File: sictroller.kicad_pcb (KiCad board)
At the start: 8 copper layers, 297 parts, among them J1 CONN_01X02, J10 CONN_01X02, J11 RINGTERM, J12 RINGTERM, J13 CONN_01X01, J2 CONN_01X08, J3 CONN_02X05, J4 RINGTERM, J5 RINGTERM, J6 RINGTERM, J7 CONN_01X02, J8 RINGTERM, J9 RINGTERM, P1 CONN_01X03, Q1 CSD17483F4, Q2 CCS050M12CM2, T1 7508110151, U1 ACPL-M61L, U10 74LVC2G04, U11 TXS0108E, U12 MGJ1, U13 MGJ1, U14 2ED020I12-F2, U15 MGJ1, U16 MGJ1, U17 2ED020I12-F2, U18 MGJ1, U19 MGJ1, U2 TMS320F28069M, U20 2ED020I12-F2, U3 ADM3053, U4 TPS76201, U5 TPS76201, U6 XCL221B18, U7 VIPER26HD, U8 ADUM5241, U9 MAX6691, Y1 CSTCE20M0V13C

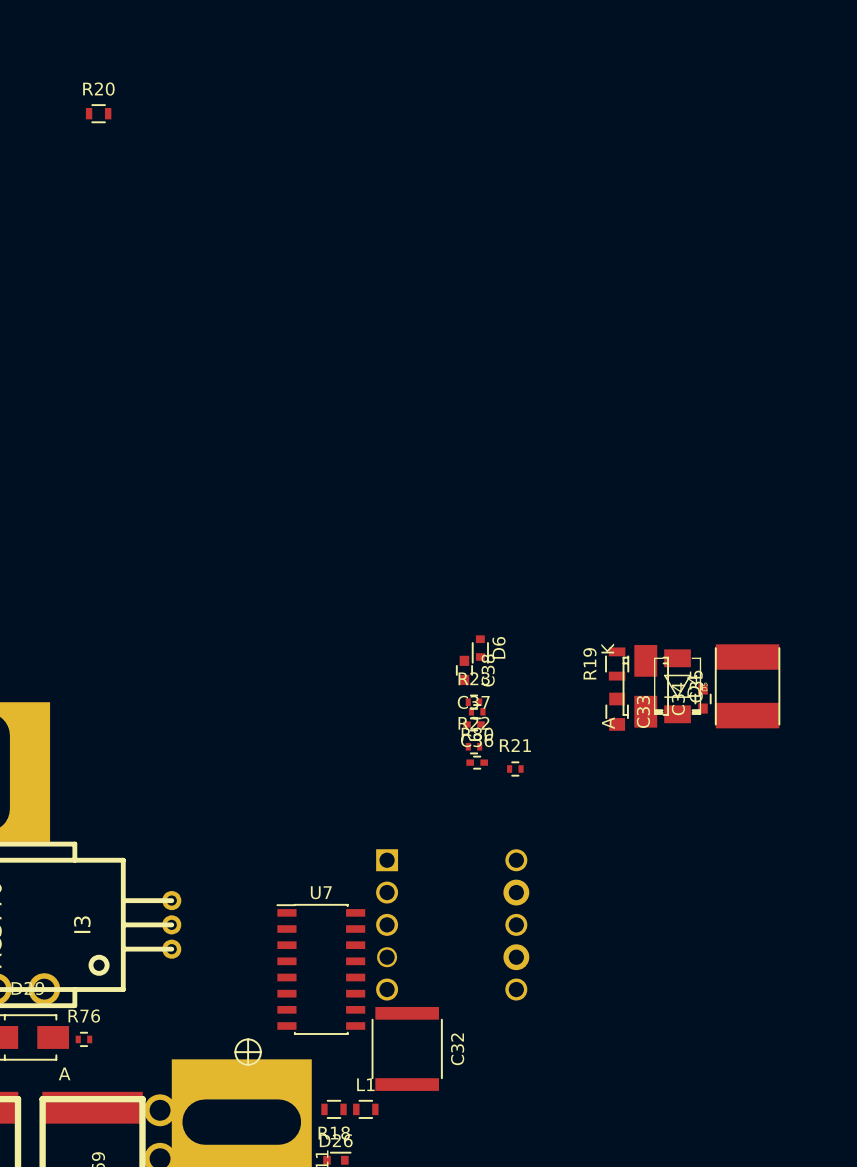
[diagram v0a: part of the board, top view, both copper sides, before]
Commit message: stepdown PSU placed
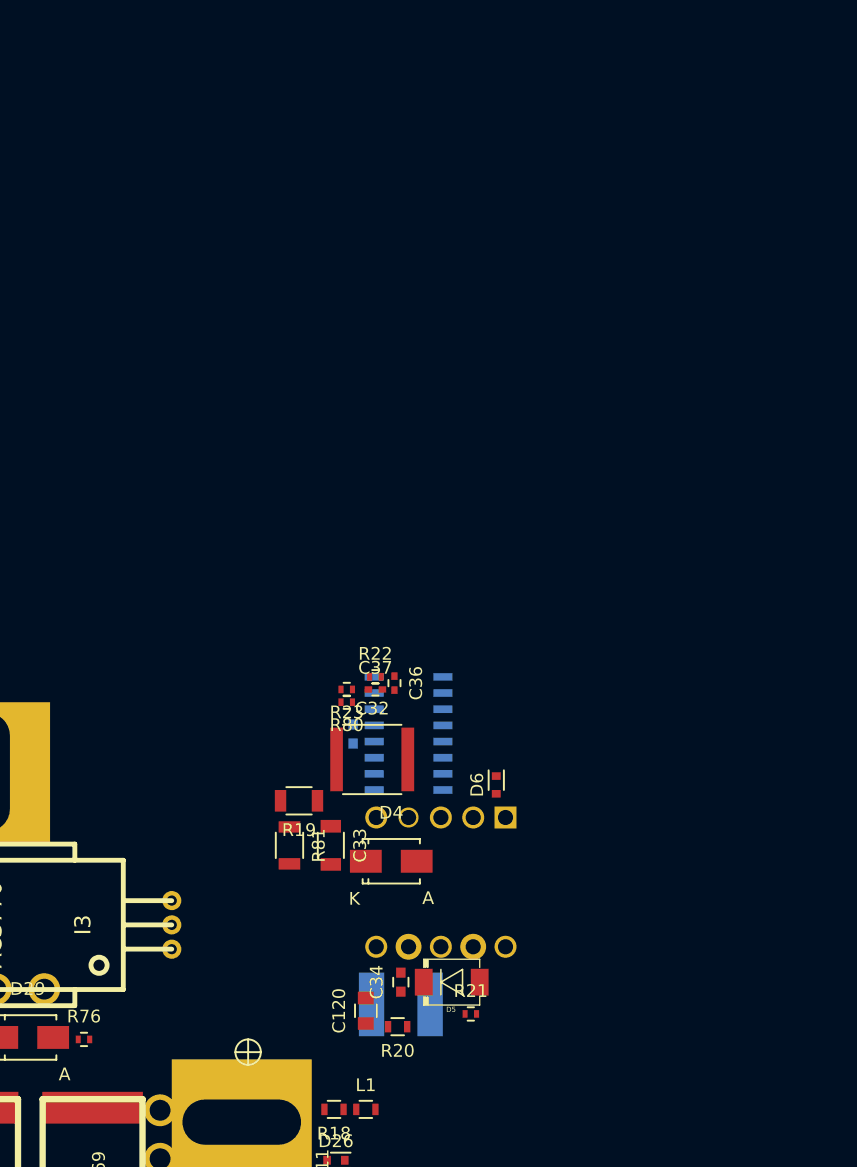
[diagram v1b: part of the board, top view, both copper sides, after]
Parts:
- added C120: 10uF 16V, Capacitors_SMD:C_0805, F.Cu at (162.2, 50.8)
- added R81: 51k, Resistors_SMD:R_1206, F.Cu at (156.2, 37.8)
- C32: value 1uF 700V -> 0.47uF 1kV
- C33: footprint Capacitors_SMD:C_0805 -> Capacitors_SMD:C_1206
- C35, C38, U7: moved to B.Cu
- R19: value 100k -> 51k; footprint Resistors_SMD:R_0805 -> Resistors_SMD:R_1206
- R20: value 0R/BEAD -> FERRITE
- moved R20 75.5 mm to (164.8, 52.0), turned to 180 degrees
- moved C35 37.0 mm to (165.0, 50.2), turned to 180 degrees
- moved C34 32.5 mm to (165.0, 48.5)
- moved D5 29.3 mm to (169.0, 48.5), turned to 0 degrees
- moved R19 27.2 mm to (157.0, 34.2), turned to 180 degrees
- moved C33 24.8 mm to (159.5, 37.8)
- moved D4 24.3 mm to (164.2, 39.0), turned to 0 degrees
- moved C32 22.9 mm to (162.8, 31.0), turned to 0 degrees
- moved U7 19.8 mm to (165.6, 29.0)
- moved R21 19.6 mm to (170.5, 51.0)
- moved D6 10.8 mm to (172.5, 33.0), turned to 90 degrees
- moved R80 10.3 mm to (160.8, 26.5)
- moved C38 10.1 mm to (161.2, 29.0)
- moved R23 10.0 mm to (160.8, 25.5), turned to 180 degrees
- moved R22 9.50 mm to (163.0, 24.5)
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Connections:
- R19 pad 2: Net-(C33-Pad2) -> Net-(R19-Pad2)
- U11 pad 9: +3V3 -> (no net)

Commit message: Add more ceralinks on rear
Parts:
- removed the R20 at (164.8, 52.0)
- added C79: 1uF, sictroller:Ceralink-L, B.Cu at (82.1, 63.1)
- added C80: 1uF, sictroller:Ceralink-L, B.Cu at (91.8, 63.1)
- added C81: 1uF, sictroller:Ceralink-L, B.Cu at (101.6, 63.1)
- added C82: 1uF, sictroller:Ceralink-L, B.Cu at (111.4, 63.1)
- added C83: 1uF, sictroller:Ceralink-L, B.Cu at (121.2, 63.1)
- added C84: 1uF, sictroller:Ceralink-L, B.Cu at (131.0, 63.1)
- added C85: 1uF, sictroller:Ceralink-L, B.Cu at (82.1, 77.0)
- added C86: 1uF, sictroller:Ceralink-L, B.Cu at (91.8, 77.0)
- added C87: 1uF, sictroller:Ceralink-L, B.Cu at (101.6, 77.0)
- added C88: 1uF, sictroller:Ceralink-L, B.Cu at (111.4, 77.0)
- added C89: 1uF, sictroller:Ceralink-L, B.Cu at (121.2, 77.0)
- added C90: 1uF, sictroller:Ceralink-L, B.Cu at (131.0, 77.0)
- added R21: FERRITE, Resistors_SMD:R_0805, F.Cu at (164.8, 52.0)
- added TH2: NCP15XW153J03RC, Resistors_SMD:R_0402, B.Cu at (106.5, 70.0)
- added W23: TEST_1P, Measurement_Points:Measurement_Point_Round-TH_Small, F.Cu at (160.8, 103.8)
- added W24: TEST_1P, Measurement_Points:Measurement_Point_Round-TH_Small, F.Cu at (170.8, 103.8)
- moved U8 165.6 mm to (163.8, 108.0)
- moved J10 160.7 mm to (164.5, 96.8)
- moved U9 158.4 mm to (164.7, 100.9)
- moved R48 151.2 mm to (164.5, 103.5)
- moved R37 30.9 mm to (62.5, -44.2)
- moved R36 28.7 mm to (58.0, -44.8)
- moved C48 18.7 mm to (59.2, -40.5)
- moved R46 10.4 mm to (89.8, -20.0)
- moved R38 8.14 mm to (91.0, -25.0)
- moved R31 6.19 mm to (87.2, -19.2)
- moved C42 4.36 mm to (62.5, -29.8)
- moved C46 3.10 mm to (62.0, -34.0)
- turned C76 to 90 degrees
- renumbered C87 to C100, C88 to C101, C89 to C102, C90 to C103, C91 to C104, C92 to C105, C93 to C106, C94 to C107, C95 to C108, C96 to C109, C97 to C110, C98 to C111, C99 to C112, C100 to C113, C101 to C114, C102 to C115, C103 to C116, C104 to C117, C105 to C118, C106 to C119, C107 to C120, C108 to C121, C109 to C122, C110 to C123, C111 to C124, C112 to C125, C113 to C126, C114 to C127, C115 to C128, C116 to C129, C117 to C130, C118 to C131, C119 to C132, C120 to C35, C35 to C36, C36 to C37, C37 to C38, C38 to C39, C39 to C40, C40 to C41, C41 to C42, C42 to C43, C43 to C44, C44 to C45, C45 to C46, C46 to C47, C47 to C48, C48 to C49, C49 to C50, C50 to C51, C51 to C52, C52 to C53, C53 to C54, C54 to C55, C55 to C56, C56 to C57, C57 to C58, C58 to C59, C59 to C60, C60 to C61, C61 to C62, C62 to C63, C63 to C64, C64 to C65, C65 to C66, C66 to C67, C67 to C68, C68 to C69, C69 to C70, C70 to C71, C71 to C72, C72 to C73, C73 to C74, C74 to C75, C75 to C76, C76 to C77, C77 to C78, C78 to C91, C79 to C92, C80 to C93, C81 to C94, C82 to C95, C83 to C96, C84 to C97, C85 to C98, C86 to C99, R81 to R20, R21 to R22, R80 to R23, R22 to R24, R23 to R25, R24 to R26, R25 to R27, R26 to R28, R27 to R29, R28 to R30, R29 to R31, R30 to R32, R31 to R33, R32 to R34, R33 to R35, R34 to R36, R35 to R37, R36 to R38, R37 to R39, R38 to R40, R39 to R41, R40 to R42, R41 to R43, R42 to R44, R43 to R45, R44 to R46, R45 to R47, R46 to R48, R47 to R49, R48 to R50, R49 to R51, R50 to R52, R51 to R53, R52 to R54, R53 to R55, R54 to R56, R55 to R57, R56 to R58, R57 to R59, R58 to R60, R59 to R61, R60 to R62, R61 to R63, R62 to R64, R63 to R65, R64 to R66, R65 to R67, R66 to R68, R67 to R69, R68 to R70, R69 to R71, R70 to R72, R71 to R73, R72 to R74, R73 to R75, R74 to R76, R75 to R77, R76 to R78, R77 to R79, R78 to R80, R79 to R81
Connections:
- TH1 pad 2: CCS_NTC_2 -> Net-(TH1-Pad2)
- U9 pad 4: Net-(TH1-Pad1) -> Net-(U9-Pad4)
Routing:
- net CCS_NTC_2: track 13.7 -> 0.00 mm
- net Net-(TH1-Pad1): track 13.7 -> 0.60 mm, vias 0 -> 1
- net Net-(TH1-Pad2): track 0.00 -> 0.60 mm, vias 0 -> 1
- added copper zone on F.Cu, net BUS+
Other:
- rule via_min_drill: 0.254 -> 0.2032
- rule via_min_size: 0.635 -> 0.381

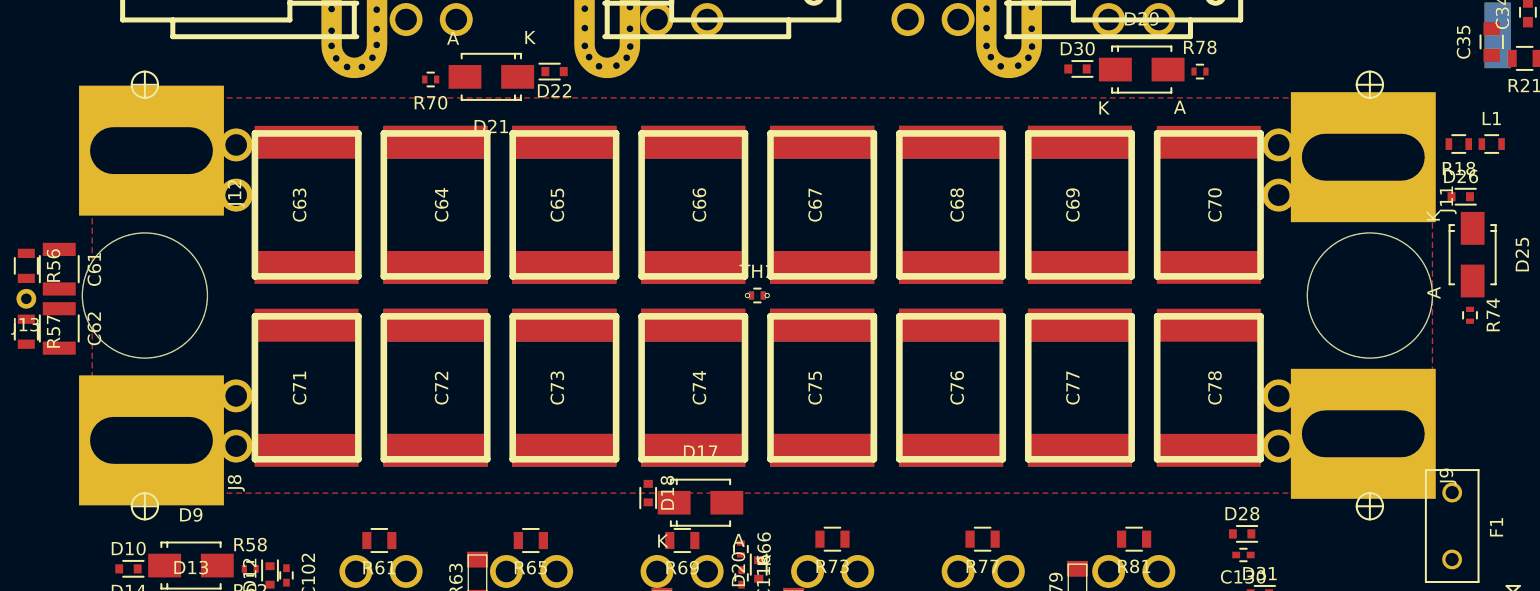
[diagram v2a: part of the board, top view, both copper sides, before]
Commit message: Add 1568 vias in DC link cap pads
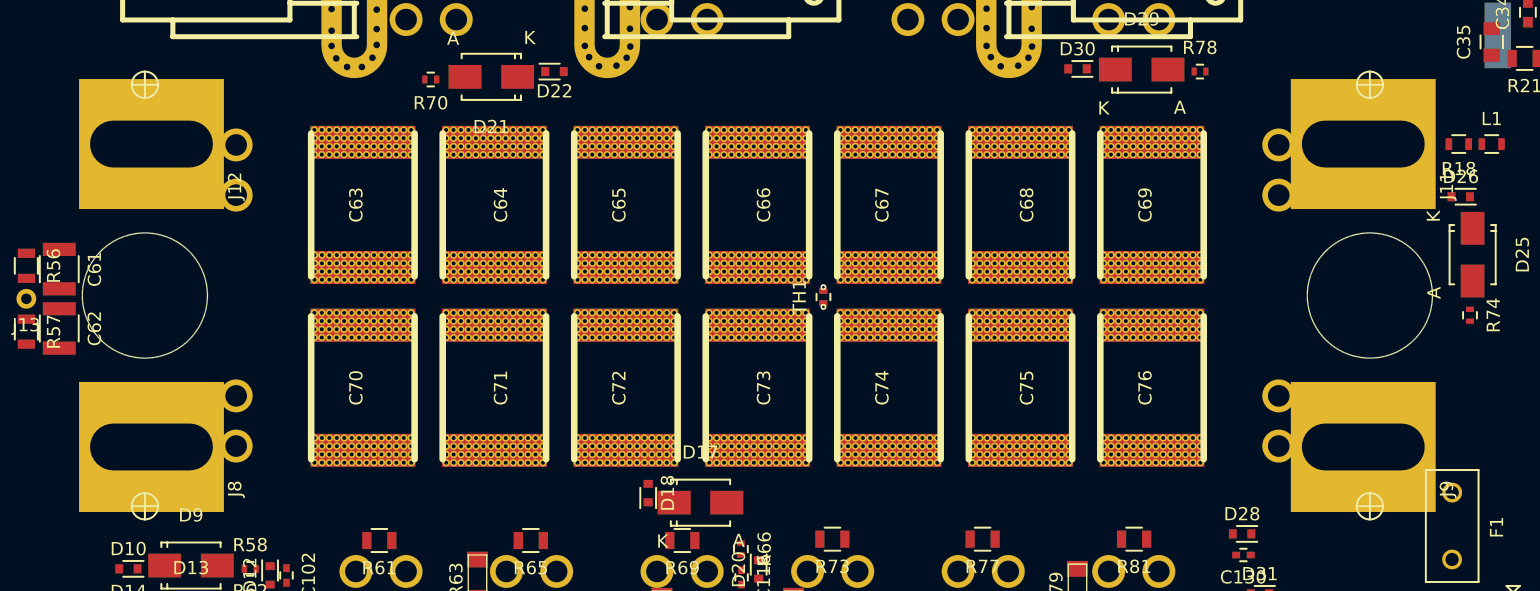
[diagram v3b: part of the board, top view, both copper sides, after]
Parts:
- C63, C64, C65, C66, C67, C68, C69, C70, C71, C72, C73, C74, C75, C76: footprint sictroller:Ceralink-L -> sictroller:Ceralink-L-viastitch
- C77, C78: moved to B.Cu
- moved C70 65.7 mm to (76.5, 77.0), turned to 270 degrees
- moved C77 56.2 mm to (76.5, 63.1)
- moved C84 56.2 mm to (76.5, 77.0)
- moved C78 56.0 mm to (86.5, 63.1)
- moved C76 15.3 mm to (136.5, 77.0), turned to 270 degrees
- moved C83 15.3 mm to (136.5, 63.1), turned to 270 degrees
- moved C75 15.1 mm to (126.5, 77.0), turned to 90 degrees
- moved C82 15.1 mm to (126.5, 63.1), turned to 90 degrees
- moved C74 14.9 mm to (116.5, 77.0), turned to 270 degrees
- moved C81 14.9 mm to (116.5, 63.1), turned to 270 degrees
- moved C73 14.7 mm to (106.5, 77.0), turned to 90 degrees
- moved C80 14.7 mm to (106.5, 63.1), turned to 90 degrees
- moved C72 14.5 mm to (96.5, 77.0), turned to 270 degrees
- moved C79 14.5 mm to (96.5, 63.1), turned to 270 degrees
- moved C71 14.3 mm to (86.5, 77.0), turned to 90 degrees
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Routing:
- removed copper zone on F.Cu, net BUS+
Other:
- copper layers 8 -> 6

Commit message: Improved footprint for B6A-PCB
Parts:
- I1, I2, I3: moved to B.Cu
- TH1, TH2: footprint Resistors_SMD:R_0402 -> sictroller:R_0402_extwire
- moved U2 264.8 mm to (107.4, 122.4), turned to 315 degrees
- moved J2 250.0 mm to (174.4, 123.8), turned to 90 degrees
- moved C19 63.6 mm to (154.4, -145.9), turned to 90 degrees
- moved P1 47.2 mm to (178.1, -143.6), turned to 90 degrees
- moved C17 47.2 mm to (168.6, -139.3), turned to 90 degrees
- moved C23 46.2 mm to (168.5, -145.6), turned to 90 degrees
- moved C22 44.6 mm to (168.4, -143.1), turned to 90 degrees
- moved C18 39.8 mm to (169.8, -135.4), turned to 90 degrees
- moved R9 34.3 mm to (171.2, -143.3), turned to 90 degrees
- moved R10 32.6 mm to (170.8, -138.6), turned to 90 degrees
- moved U1 27.4 mm to (189.2, -156.3)
- moved D18 11.4 mm to (109.5, 86.1)
- moved J5 6.36 mm to (101.4, 38.4)
- moved J4 6.24 mm to (69.6, 38.2)
- moved J6 6.15 mm to (131.9, 38.1)
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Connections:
- I1 pad 4: PHASE_A -> /Feedback/A
- I1 pad 5: /Feedback/A -> PHASE_A
- I2 pad 4: /Feedback/B -> PHASE_B
- I2 pad 5: PHASE_B -> /Feedback/B
- I3 pad 4: /Feedback/C -> PHASE_C
- I3 pad 5: PHASE_C -> /Feedback/C
- TH2 pad 1: Net-(TH1-Pad1) -> Net-(TH2-Pad1)
- TH2 pad 2: Net-(TH1-Pad2) -> Net-(TH2-Pad2)
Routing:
- net Net-(TH1-Pad2): track 0.60 -> 0.01 mm, vias 1 -> 0
- net Net-(TH1-Pad1): track 0.60 -> 0.05 mm, vias 1 -> 0
- added copper zone on F.Cu, net BUS+
- added copper zone on In2.Cu, net BUS+
- added copper zone on In4.Cu, net BUS+
- added copper zone on B.Cu, net BUS-
- added copper zone on In1.Cu, net BUS-
- added copper zone on In3.Cu, net BUS-

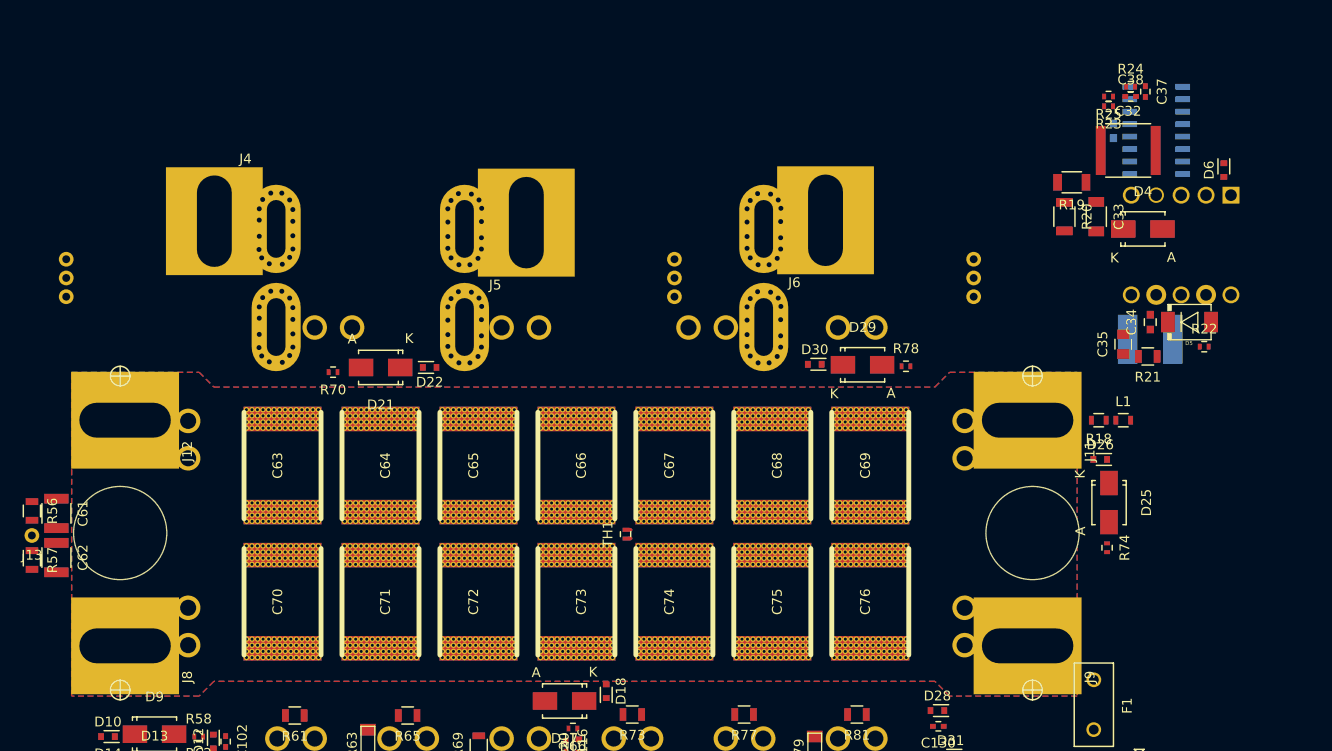
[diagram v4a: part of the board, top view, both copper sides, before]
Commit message: phase connection tweaks
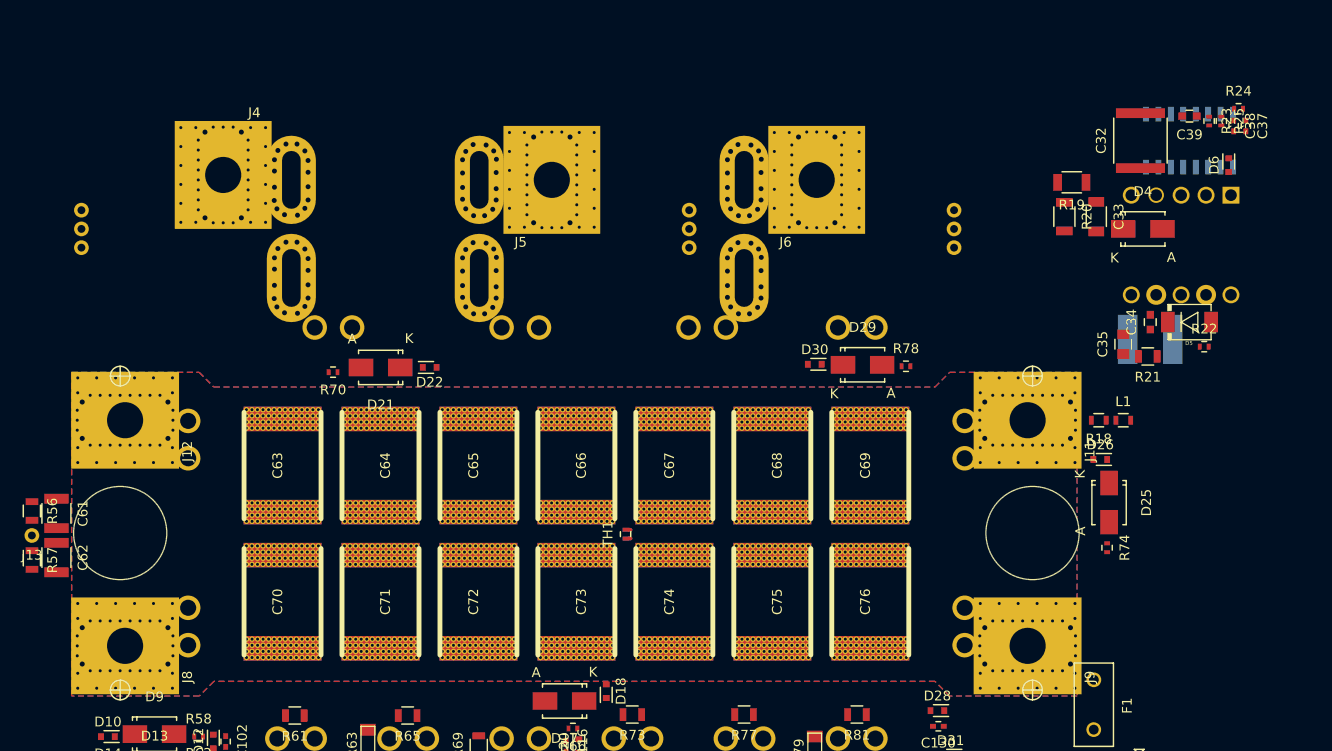
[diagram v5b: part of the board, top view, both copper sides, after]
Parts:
- C39: moved to F.Cu
- moved R25 11.8 mm to (172.2, 28.0), turned to 270 degrees
- moved R24 11.2 mm to (174.0, 26.8)
- moved C38 10.9 mm to (173.5, 28.5), turned to 270 degrees
- moved C37 10.8 mm to (174.8, 28.5)
- moved R23 10.4 mm to (171.0, 28.0), turned to 270 degrees
- moved C39 7.89 mm to (169.0, 27.5), turned to 180 degrees
- moved I3 5.39 mm to (145.0, 39.0)
- moved I1 5.23 mm to (56.0, 39.0)
- moved I2 5.22 mm to (118.0, 39.0)
- moved J5 5.08 mm to (104.0, 34.0)
- moved J4 4.80 mm to (70.5, 33.5)
- moved J6 4.22 mm to (131.0, 34.0)
- moved U7 3.55 mm to (169.0, 30.0), turned to 270 degrees
- moved C32 1.60 mm to (164.0, 30.0), turned to 90 degrees
- moved D6 0.71 mm to (173.0, 32.5)
